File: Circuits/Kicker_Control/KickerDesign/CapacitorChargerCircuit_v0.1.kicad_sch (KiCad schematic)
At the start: 8 parts, among them Q2 NMOS

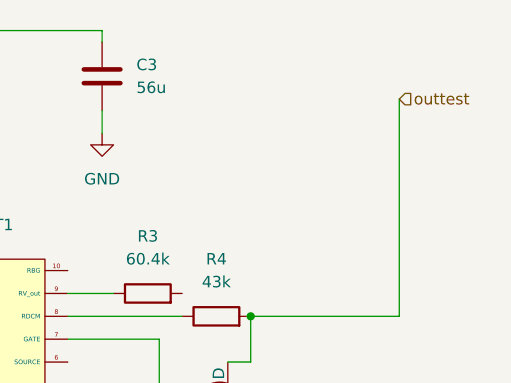
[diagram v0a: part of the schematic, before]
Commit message: Changed the Kicker subcircuit link
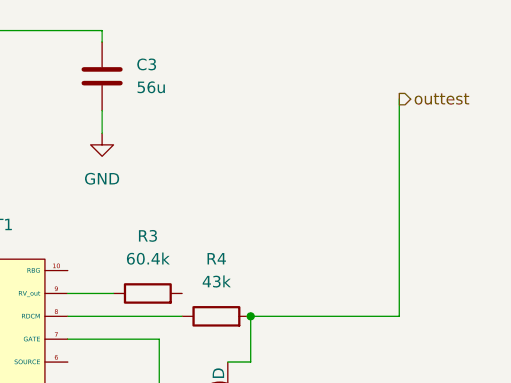
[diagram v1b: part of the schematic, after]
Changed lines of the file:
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@@
 	)
 	(hierarchical_label "outtest"
-		(shape input)
+		(shape output)
 		(at 189.23 68.58 0)
 		(fields_autoplaced yes)
@@
 		(instances
 			(project ""
-				(path "/a7a112f4-0a48-49be-a5c8-a832ec6f12fb/d53044a6-8882-4c0b-a6e2-5a56de409c7c"
+				(path "/a7a112f4-0a48-49be-a5c8-a832ec6f12fb/34d36afa-17bc-4d5b-982e-06ce0cee35e6"
 					(reference "Q2")
 					(unit 1)
@@
 		(instances
 			(project ""
-				(path "/a7a112f4-0a48-49be-a5c8-a832ec6f12fb/d53044a6-8882-4c0b-a6e2-5a56de409c7c"
+				(path "/a7a112f4-0a48-49be-a5c8-a832ec6f12fb/34d36afa-17bc-4d5b-982e-06ce0cee35e6"
 					(reference "C2")
 					(unit 1)
@@
 		(instances
 			(project "KickerCircuit_v01"
-				(path "/a7a112f4-0a48-49be-a5c8-a832ec6f12fb/d53044a6-8882-4c0b-a6e2-5a56de409c7c"
+				(path "/a7a112f4-0a48-49be-a5c8-a832ec6f12fb/34d36afa-17bc-4d5b-982e-06ce0cee35e6"
 					(reference "#PWR06")
 					(unit 1)
@@
 		(instances
 			(project "KickerCircuit_v01"
-				(path "/a7a112f4-0a48-49be-a5c8-a832ec6f12fb/d53044a6-8882-4c0b-a6e2-5a56de409c7c"
+				(path "/a7a112f4-0a48-49be-a5c8-a832ec6f12fb/34d36afa-17bc-4d5b-982e-06ce0cee35e6"
 					(reference "#PWR07")
 					(unit 1)
@@
 		(instances
 			(project "KickerCircuit_v01"
-				(path "/a7a112f4-0a48-49be-a5c8-a832ec6f12fb/d53044a6-8882-4c0b-a6e2-5a56de409c7c"
+				(path "/a7a112f4-0a48-49be-a5c8-a832ec6f12fb/34d36afa-17bc-4d5b-982e-06ce0cee35e6"
 					(reference "R4")
 					(unit 1)
@@
 		(instances
 			(project ""
-				(path "/a7a112f4-0a48-49be-a5c8-a832ec6f12fb/d53044a6-8882-4c0b-a6e2-5a56de409c7c"
+				(path "/a7a112f4-0a48-49be-a5c8-a832ec6f12fb/34d36afa-17bc-4d5b-982e-06ce0cee35e6"
 					(reference "R3")
 					(unit 1)
@@
 		(instances
 			(project ""
-				(path "/a7a112f4-0a48-49be-a5c8-a832ec6f12fb/d53044a6-8882-4c0b-a6e2-5a56de409c7c"
+				(path "/a7a112f4-0a48-49be-a5c8-a832ec6f12fb/34d36afa-17bc-4d5b-982e-06ce0cee35e6"
 					(reference "#PWR05")
 					(unit 1)
@@
 		(instances
 			(project "KickerCircuit_v01"
-				(path "/a7a112f4-0a48-49be-a5c8-a832ec6f12fb/d53044a6-8882-4c0b-a6e2-5a56de409c7c"
+				(path "/a7a112f4-0a48-49be-a5c8-a832ec6f12fb/34d36afa-17bc-4d5b-982e-06ce0cee35e6"
 					(reference "C3")
 					(unit 1)
@@
 		(instances
 			(project "KickerCircuit_v01"
-				(path "/a7a112f4-0a48-49be-a5c8-a832ec6f12fb/d53044a6-8882-4c0b-a6e2-5a56de409c7c"
+				(path "/a7a112f4-0a48-49be-a5c8-a832ec6f12fb/34d36afa-17bc-4d5b-982e-06ce0cee35e6"
 					(reference "#PWR08")
 					(unit 1)
@@
 		(instances
 			(project "KickerCircuit_v01"
-				(path "/a7a112f4-0a48-49be-a5c8-a832ec6f12fb/d53044a6-8882-4c0b-a6e2-5a56de409c7c"
+				(path "/a7a112f4-0a48-49be-a5c8-a832ec6f12fb/34d36afa-17bc-4d5b-982e-06ce0cee35e6"
 					(reference "C4")
 					(unit 1)
@@
 		(instances
 			(project "KickerCircuit_v01"
-				(path "/a7a112f4-0a48-49be-a5c8-a832ec6f12fb/d53044a6-8882-4c0b-a6e2-5a56de409c7c"
+				(path "/a7a112f4-0a48-49be-a5c8-a832ec6f12fb/34d36afa-17bc-4d5b-982e-06ce0cee35e6"
 					(reference "R5")
 					(unit 1)
@@
 		(instances
 			(project ""
-				(path "/a7a112f4-0a48-49be-a5c8-a832ec6f12fb/d53044a6-8882-4c0b-a6e2-5a56de409c7c"
+				(path "/a7a112f4-0a48-49be-a5c8-a832ec6f12fb/34d36afa-17bc-4d5b-982e-06ce0cee35e6"
 					(reference "LT1")
 					(unit 1)
@@
 		)
 	)
-	(sheet_instances
-		(path "/"
-			(page "1")
-		)
-	)

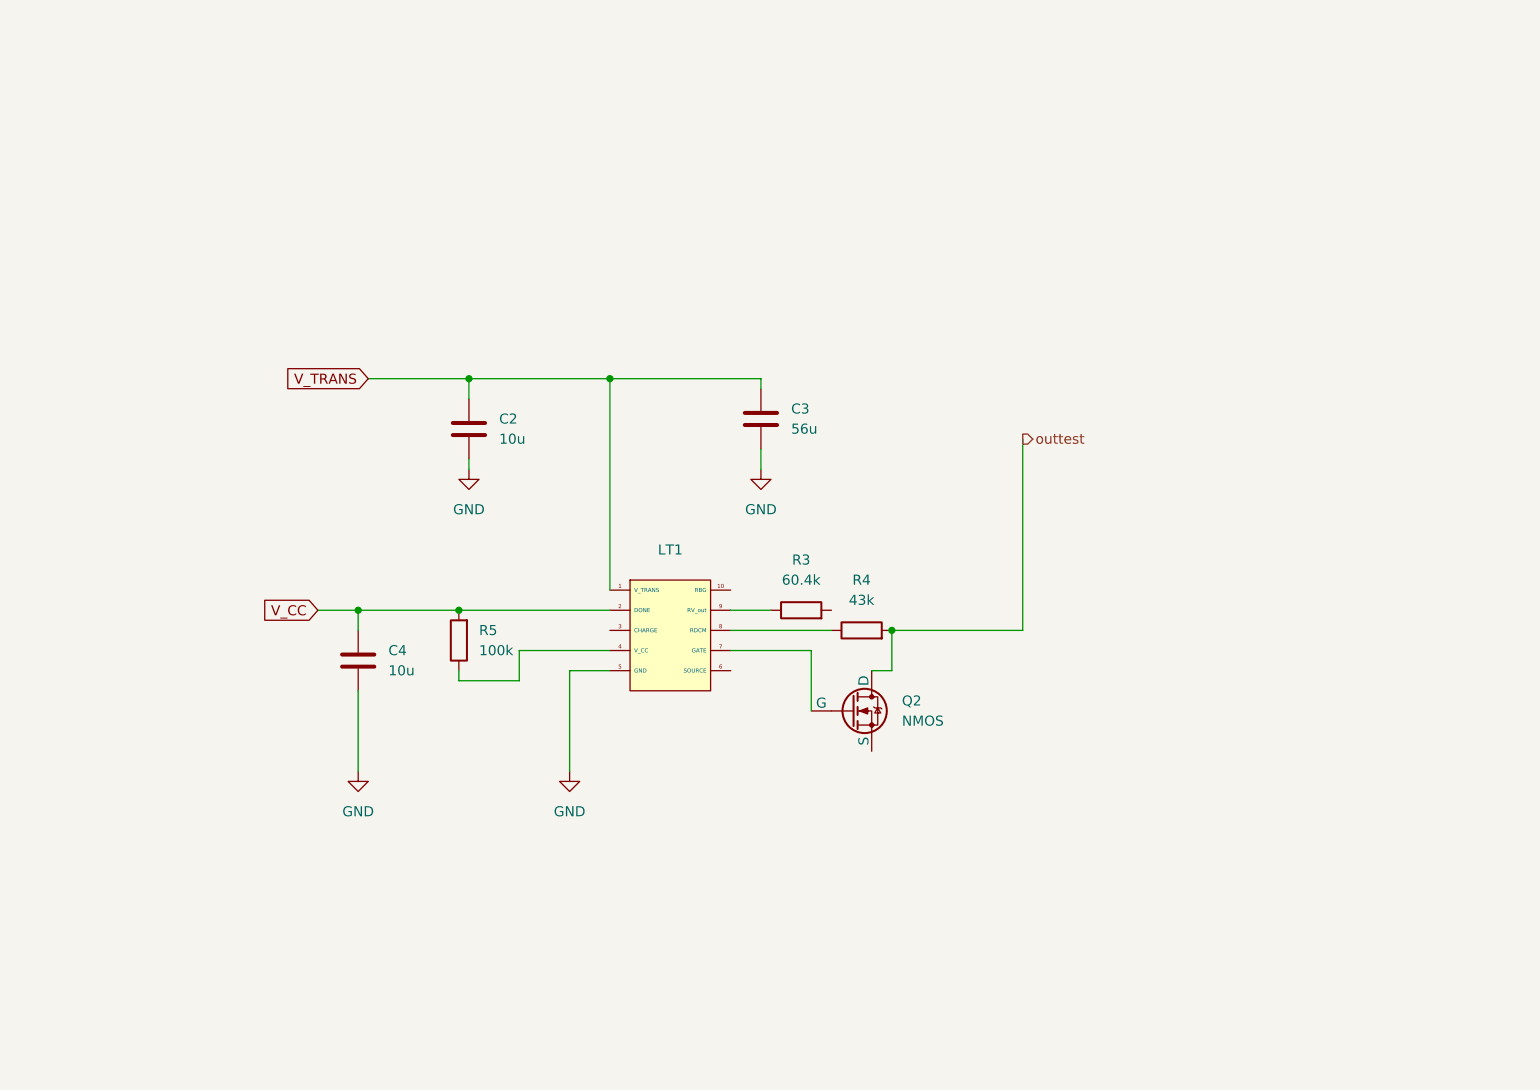
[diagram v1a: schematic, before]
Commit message: Updated the Capacitor Charger Circuit
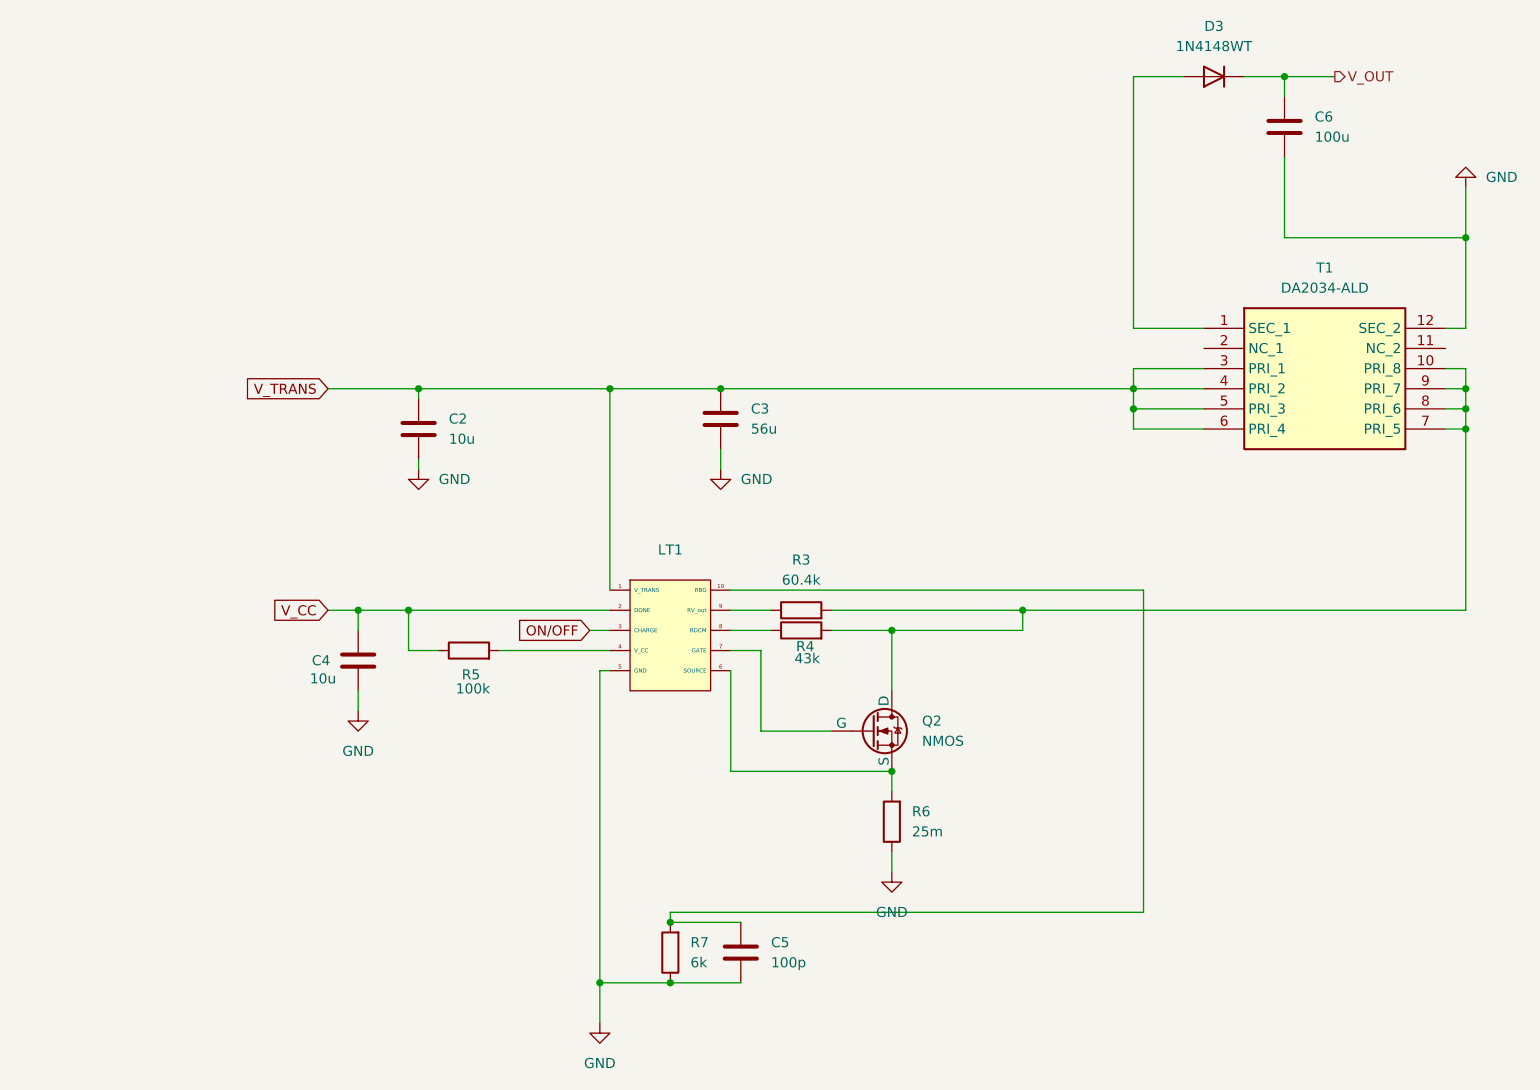
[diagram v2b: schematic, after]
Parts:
- added C5: 100p, symbol Device:C
- added C6: 100u, symbol Device:C
- added D3: 1N4148WT, Diode_SMD:D_SOD-523, symbol Diode:1N4148WT
- added R6: 25m, symbol Device:R
- added R7: 6k, symbol Device:R
- added T1: DA2034-ALD, SOP300P3000X1143-12N, symbol DA2034-ALD:DA2034-ALD
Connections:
- net outtest is gone; now on an unnamed net: Q2.1 (D), R4.2
- net GND: now also C5.2, C6.1, R6.1, R7.1, T1.12 (SEC_2)
- net V_CC: now also R5.1; no longer R5.2
- net V_TRANS: now also T1.3 (PRI_1), T1.4 (PRI_2), T1.5 (PRI_3), T1.6 (PRI_4)
- net at Q2.3 (S): now also LT1.6 (SOURCE), R6.2
- net at R3.2: now also T1.10 (PRI_8), T1.7 (PRI_5), T1.8 (PRI_6), T1.9 (PRI_7)
- net at LT1.4 (V_CC): now also R5.2; no longer R5.1
- net at LT1.10 (RBG): now also C5.1, R7.2
- net ON/OFF: now reaches LT1.3 (CHARGE)
- new net: D3.2 (A), T1.1 (SEC_1)
- new net V_OUT: C6.2, D3.1 (K)
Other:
- moved on the sheet: C2, C3, Q2, R4, R5

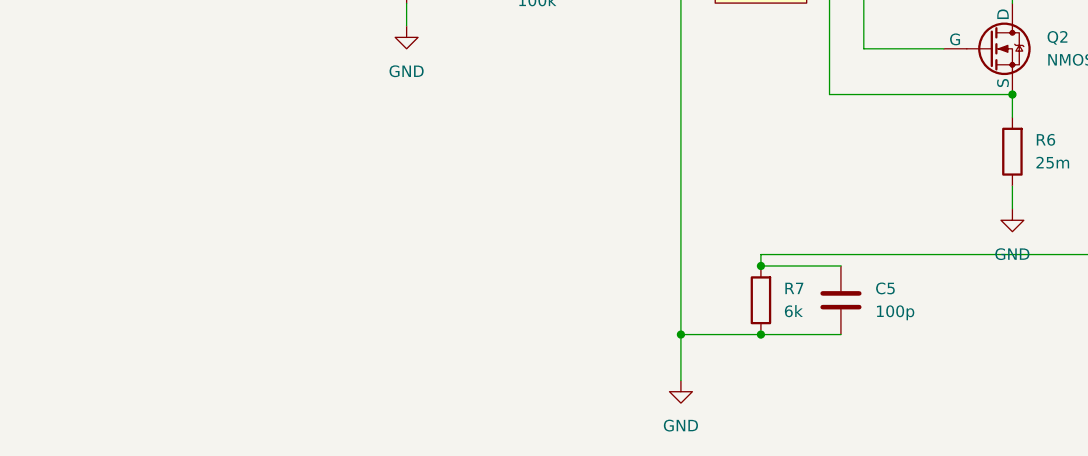
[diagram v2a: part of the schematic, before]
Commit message: Updated the Capacitor Charger Circuit
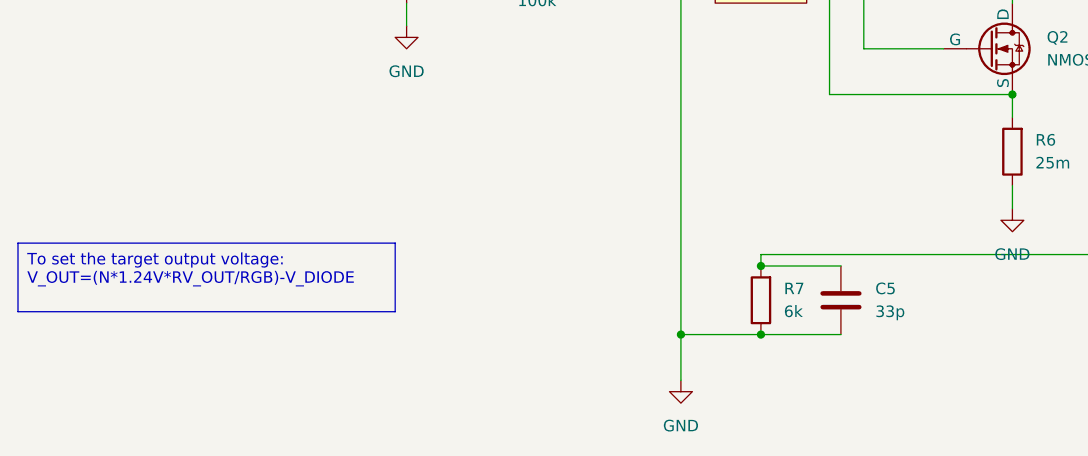
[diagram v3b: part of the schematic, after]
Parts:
- C5: value 100p -> 33p
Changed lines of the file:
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@@
+		)
+	)
+	(text_box "To set the target output voltage: \nV_OUT=(N*1.24V*RV_OUT/RGB)-V_DIODE"
+		(exclude_from_sim no)
+		(at 62.23 127 0)
+		(size 41.91 7.62)
+		(stroke
+			(width 0)
+			(type default)
+		)
+		(fill
+			(type none)
+		)
+		(effects
+			(font
+				(size 1.27 1.27)
+			)
+			(justify left top)
 		)
 	)
@@
 			)
 		)
-		(property "Value" "100p"
+		(property "Value" "33p"
 			(at 157.48 134.6199 0)
 			(effects
@@
 		)
 	)
+	(sheet_instances
+		(path "/"
+			(page "1")
+		)
+	)
